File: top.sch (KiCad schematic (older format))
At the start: 3 parts

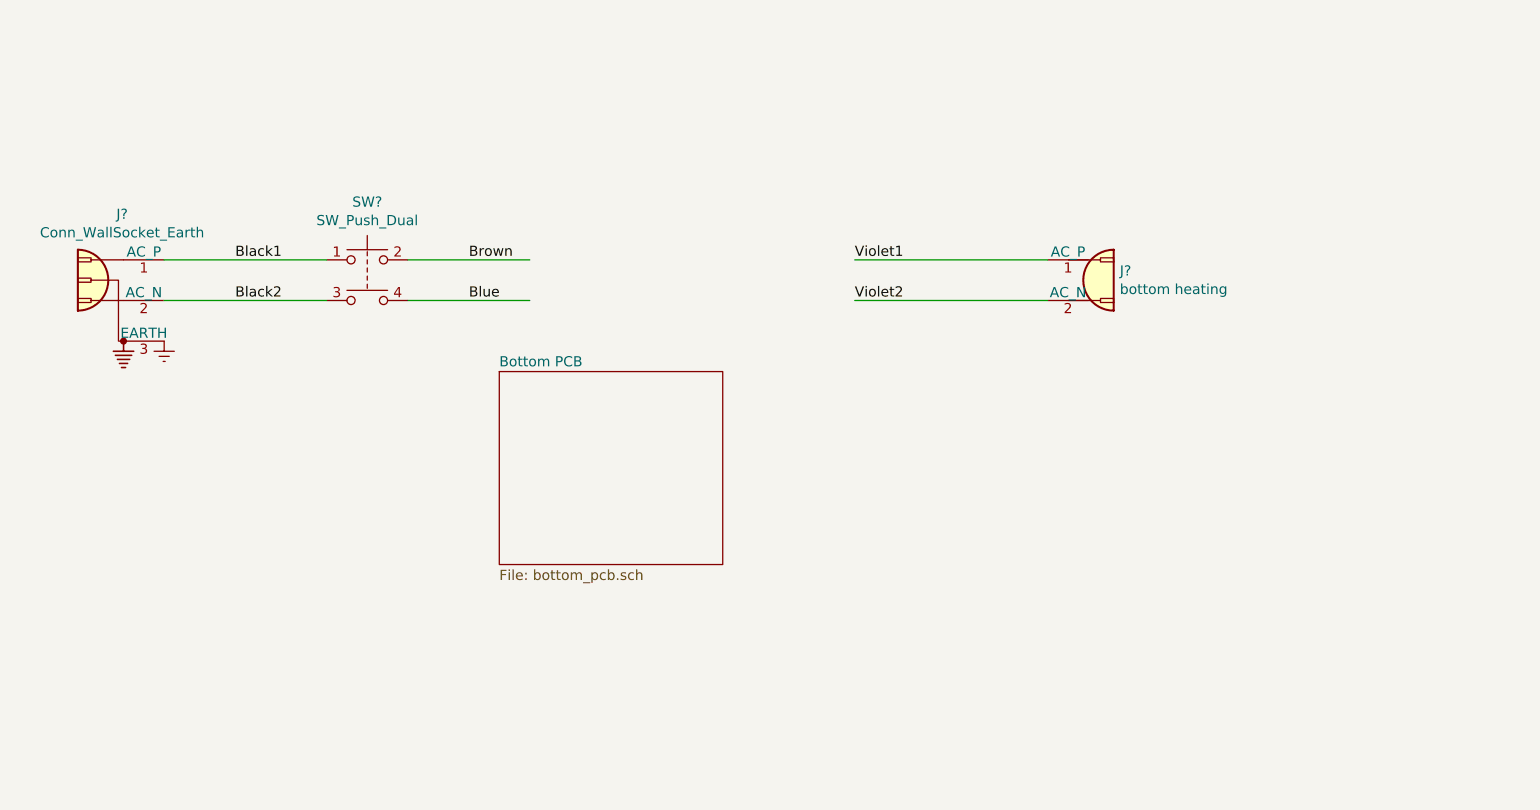
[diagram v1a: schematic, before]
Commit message: Added D-Sub 9 connector
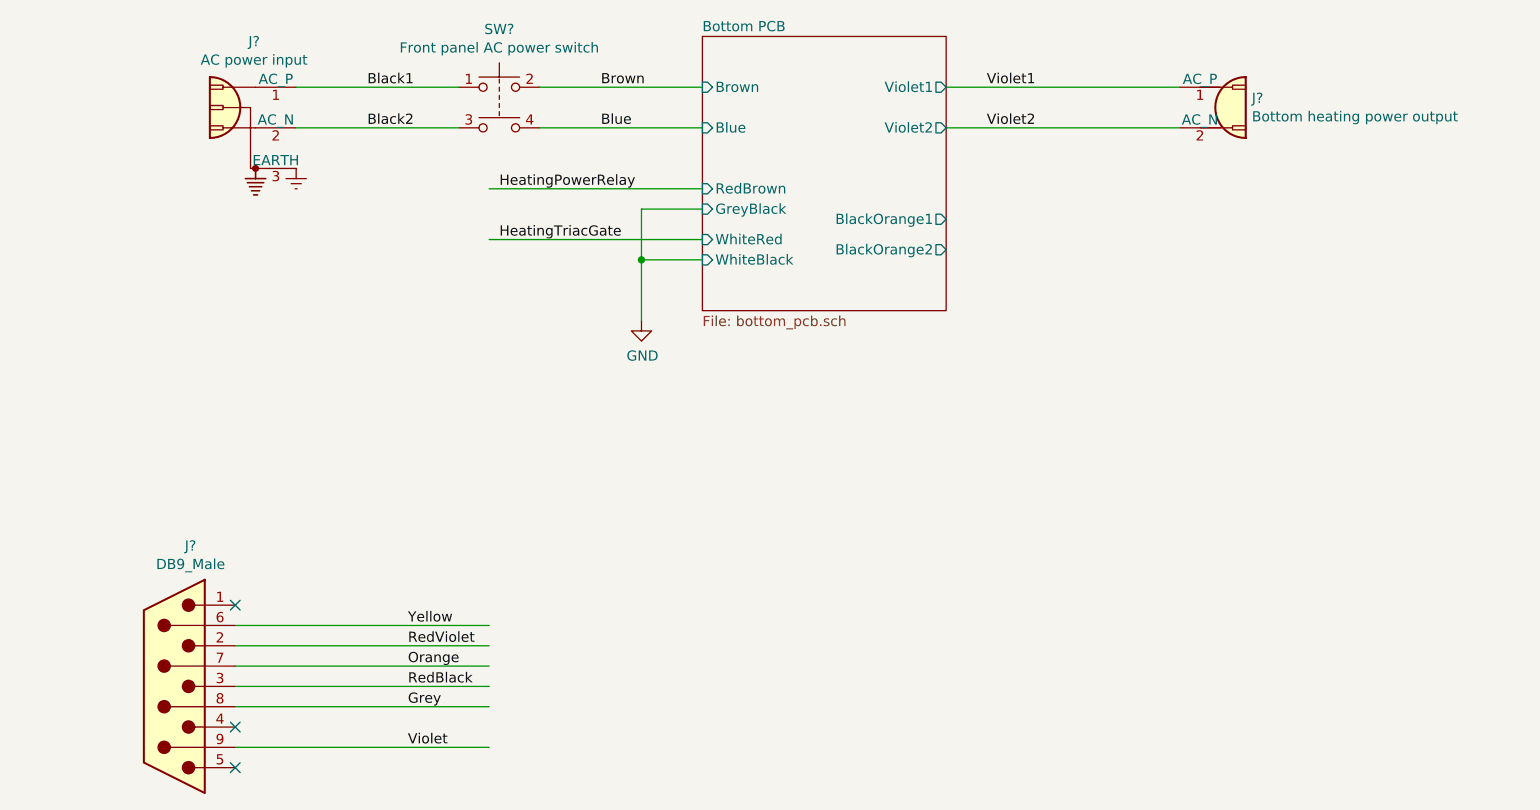
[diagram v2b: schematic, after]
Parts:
- added J?: DB9_Male, symbol Connector:DB9_Male
- J?: value Conn_WallSocket_Earth -> AC power input
- J?: value bottom heating -> Bottom heating power output
- SW?: value SW_Push_Dual -> Front panel AC power switch
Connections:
- net labels added: GND, Grey, HeatingPowerRelay, HeatingTriacGate, Orange, RedBlack, RedViolet, Violet, Yellow
- wire segments 6 -> 18
- no-connect marks 0 -> 3
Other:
- moved on the sheet: J?, SW?
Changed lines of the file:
@@
 L Connector:Conn_WallSocket_Earth J?
 U 1 1 5BD76A45
-P 2250 2600
-F 0 "J?" H 2257 3025 50  0000 C CNN
-F 1 "Conn_WallSocket_Earth" H 2257 2934 50  0000 C CNN
-F 2 "" H 1950 2700 50  0001 C CNN
-F 3 "~" H 1950 2700 50  0001 C CNN
-	1    2250 2600
+P 2900 1750
+F 0 "J?" H 2907 2175 50  0000 C CNN
+F 1 "AC power input" H 2907 2084 50  0000 C CNN
+F 2 "" H 2600 1850 50  0001 C CNN
+F 3 "~" H 2600 1850 50  0001 C CNN
+	1    2900 1750
 	-1   0    0    -1
 $EndComp
@@
 L Connector:Conn_WallSocket J?
 U 1 1 5BD76B88
-P 7000 2500
-F 0 "J?" H 7155 2546 50  0000 L CNN
-F 1 "bottom heating" H 7155 2455 50  0000 L CNN
-F 2 "" H 6600 2500 50  0001 C CNN
-F 3 "~" H 6600 2500 50  0001 C CNN
-	1    7000 2500
+P 7650 1650
+F 0 "J?" H 7805 1696 50  0000 L CNN
+F 1 "Bottom heating power output" H 7805 1605 50  0000 L CNN
+F 2 "" H 7250 1650 50  0001 C CNN
+F 3 "~" H 7250 1650 50  0001 C CNN
+	1    7650 1650
 	1    0    0    -1
 $EndComp
 Wire Wire Line
-	6800 2400 5850 2400
+	7450 1550 6300 1550
 Wire Wire Line
-	6800 2600 5850 2600
-Text Label 5850 2400 0    50   ~ 0
+	7450 1750 6300 1750
+Text Label 6500 1550 0    50   ~ 0
 Violet1
-Text Label 5850 2600 0    50   ~ 0
+Text Label 6500 1750 0    50   ~ 0
 Violet2
 Wire Wire Line
-	2450 2400 3250 2400
+	3100 1550 3900 1550
 Wire Wire Line
-	2450 2600 3250 2600
-Text Label 2800 2400 0    50   ~ 0
+	3100 1750 3900 1750
+Text Label 3450 1550 0    50   ~ 0
 Black1
-Text Label 2800 2600 0    50   ~ 0
+Text Label 3450 1750 0    50   ~ 0
 Black2
 $Comp
 L Switch:SW_Push_Dual SW?
 U 1 1 5BD77280
-P 3450 2400
-F 0 "SW?" H 3450 2685 50  0000 C CNN
-F 1 "SW_Push_Dual" H 3450 2594 50  0000 C CNN
-F 2 "" H 3450 2600 50  0001 C CNN
-F 3 "" H 3450 2600 50  0001 C CNN
-	1    3450 2400
+P 4100 1550
+F 0 "SW?" H 4100 1835 50  0000 C CNN
+F 1 "Front panel AC power switch" H 4100 1744 50  0000 C CNN
+F 2 "" H 4100 1750 50  0001 C CNN
+F 3 "" H 4100 1750 50  0001 C CNN
+	1    4100 1550
 	1    0    0    -1
 $EndComp
 Wire Wire Line
-	3650 2400 4250 2400
+	4300 1550 5100 1550
 Wire Wire Line
-	3650 2600 4250 2600
-Text Label 3950 2400 0    50   ~ 0
+	4300 1750 5100 1750
+Text Label 4600 1550 0    50   ~ 0
 Brown
-Text Label 3950 2600 0    50   ~ 0
+Text Label 4600 1750 0    50   ~ 0
 Blue
 $Comp
 L power:Earth #PWR?
 U 1 1 5BD774C6
-P 2450 2800
-F 0 "#PWR?" H 2450 2550 50  0001 C CNN
-F 1 "Earth" H 2450 2650 50  0001 C CNN
-F 2 "" H 2450 2800 50  0001 C CNN
-F 3 "~" H 2450 2800 50  0001 C CNN
-	1    2450 2800
+P 3100 1950
+F 0 "#PWR?" H 3100 1700 50  0001 C CNN
+F 1 "Earth" H 3100 1800 50  0001 C CNN
+F 2 "" H 3100 1950 50  0001 C CNN
+F 3 "~" H 3100 1950 50  0001 C CNN
+	1    3100 1950
 	1    0    0    -1
 $EndComp
 $Sheet
-S 4100 2950 1100 950
+S 5100 1300 1200 1350
 U 5BD775AF
 F0 "Bottom PCB" 50
 F1 "bottom_pcb.sch" 50
+F2 "Blue" I L 5100 1750 50
+F3 "Brown" I L 5100 1550 50
+F4 "Violet1" O R 6300 1550 50
+F5 "Violet2" O R 6300 1750 50
+F6 "GreyBlack" I L 5100 2150 50
+F7 "RedBrown" I L 5100 2050 50
+F8 "WhiteBlack" I L 5100 2400 50
+F9 "WhiteRed" I L 5100 2300 50
+F10 "BlackOrange1" O R 6300 2200 50
+F11 "BlackOrange2" O R 6300 2350 50
 $EndSheet
+$Comp
+L power:GND #PWR?
+U 1 1 5BD89AAD
+P 4800 2700
+F 0 "#PWR?" H 4800 2450 50  0001 C CNN
+F 1 "GND" H 4805 2527 50  0000 C CNN
+F 2 "" H 4800 2700 50  0001 C CNN
+F 3 "" H 4800 2700 50  0001 C CNN
+	1    4800 2700
+	1    0    0    -1
+$EndComp
+Wire Wire Line
+	4800 2700 4800 2400
+Wire Wire Line
+	4800 2150 5100 2150
+Wire Wire Line
+	5100 2400 4800 2400
+Connection ~ 4800 2400
+Wire Wire Line
+	4800 2400 4800 2150
+Wire Wire Line
+	4050 2300 5100 2300
+Text Label 4100 2300 0    50   ~ 0
+HeatingTriacGate
+Wire Wire Line
+	5100 2050 4050 2050
+Text Label 4100 2050 0    50   ~ 0
+HeatingPowerRelay
+$Comp
+L Connector:DB9_Male J?
+U 1 1 5BD8BC42
+P 2500 4500
+F 0 "J?" H 2420 3808 50  0000 C CNN
+F 1 "DB9_Male" H 2420 3899 50  0000 C CNN
+F 2 "" H 2500 4500 50  0001 C CNN
+F 3 " ~" H 2500 4500 50  0001 C CNN
+	1    2500 4500
+	-1   0    0    1
+$EndComp
+NoConn ~ 2800 4100
+Wire Wire Line
+	2800 4300 4050 4300
+Text Label 3650 4300 0    50   ~ 0
+RedViolet
+Wire Wire Line
+	2800 4500 4050 4500
+Text Label 3650 4500 0    50   ~ 0
+RedBlack
+NoConn ~ 2800 4700
+NoConn ~ 2800 4900
+Wire Wire Line
+	2800 4200 4050 4200
+Text Label 3650 4200 0    50   ~ 0
+Yellow
+Wire Wire Line
+	2800 4400 4050 4400
+Text Label 3650 4400 0    50   ~ 0
+Orange
+Wire Wire Line
+	2800 4600 4050 4600
+Text Label 3650 4600 0    50   ~ 0
+Grey
+Wire Wire Line
+	2800 4800 4050 4800
+Text Label 3650 4800 0    50   ~ 0
+Violet
 $EndSCHEMATC

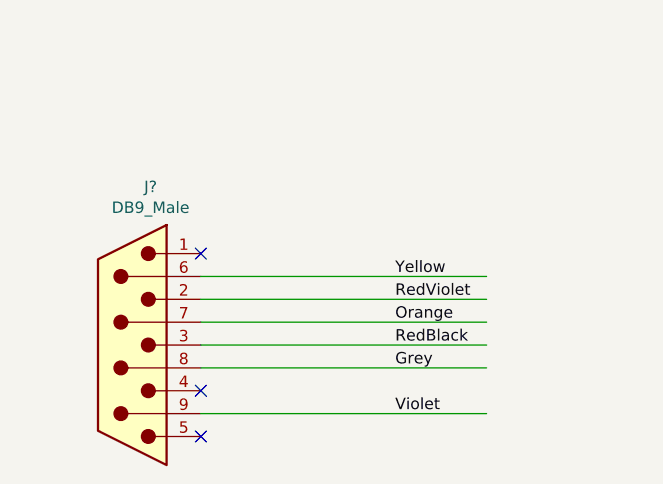
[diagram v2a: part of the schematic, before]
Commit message: Added schematic sheet for control input
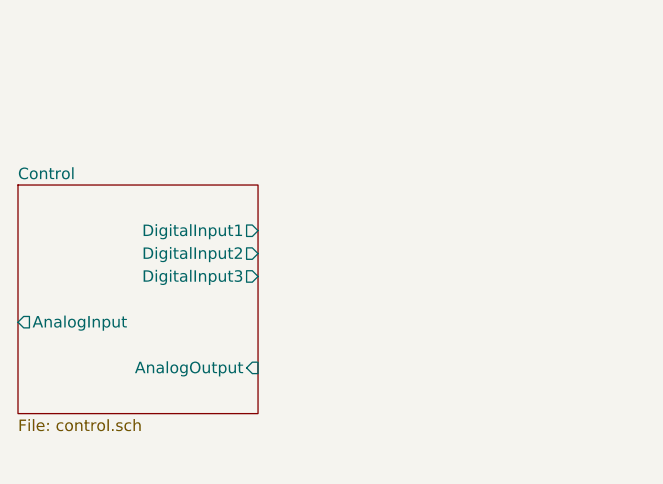
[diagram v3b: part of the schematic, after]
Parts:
- removed J?: DB9_Male, symbol Connector:DB9_Male
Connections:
- net labels removed: Grey, Orange, RedBlack, RedViolet, Violet, Yellow
- wire segments 18 -> 12
- no-connect marks 3 -> 0
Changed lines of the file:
@@
 $Descr A4 11693 8268
 encoding utf-8
-Sheet 1 2
+Sheet 1 3
 Title ""
 Date ""
@@
 Text Label 4100 2050 0    50   ~ 0
 HeatingPowerRelay
-$Comp
-L Connector:DB9_Male J?
-U 1 1 5BD8BC42
-P 2500 4500
-F 0 "J?" H 2420 3808 50  0000 C CNN
-F 1 "DB9_Male" H 2420 3899 50  0000 C CNN
-F 2 "" H 2500 4500 50  0001 C CNN
-F 3 " ~" H 2500 4500 50  0001 C CNN
-	1    2500 4500
-	-1   0    0    1
-$EndComp
-NoConn ~ 2800 4100
-Wire Wire Line
-	2800 4300 4050 4300
-Text Label 3650 4300 0    50   ~ 0
-RedViolet
-Wire Wire Line
-	2800 4500 4050 4500
-Text Label 3650 4500 0    50   ~ 0
-RedBlack
-NoConn ~ 2800 4700
-NoConn ~ 2800 4900
-Wire Wire Line
-	2800 4200 4050 4200
-Text Label 3650 4200 0    50   ~ 0
-Yellow
-Wire Wire Line
-	2800 4400 4050 4400
-Text Label 3650 4400 0    50   ~ 0
-Orange
-Wire Wire Line
-	2800 4600 4050 4600
-Text Label 3650 4600 0    50   ~ 0
-Grey
-Wire Wire Line
-	2800 4800 4050 4800
-Text Label 3650 4800 0    50   ~ 0
-Violet
+$Sheet
+S 2000 3800 1050 1000
+U 5BD88E6B
+F0 "Control" 50
+F1 "control.sch" 50
+F2 "DigitalInput1" O R 3050 4000 50
+F3 "DigitalInput2" O R 3050 4100 50
+F4 "DigitalInput3" O R 3050 4200 50
+F5 "AnalogInput" O L 2000 4400 50
+F6 "AnalogOutput" I R 3050 4600 50
+$EndSheet
 $EndSCHEMATC
